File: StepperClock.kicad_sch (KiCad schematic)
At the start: 24 parts, among them J1 Hour1, J2 Hour0, J3 Minute1, J4 Minute0, J5 Second1, J6 Second0, J7 +12V, SW1 TZ, U1 TFT Display, U10 RaspberryPi_Pico, U2 5V, U4 Hour1, U5 Hour0, U6 Min1, U7 Min0, U8 Sec1, U9 Sec0

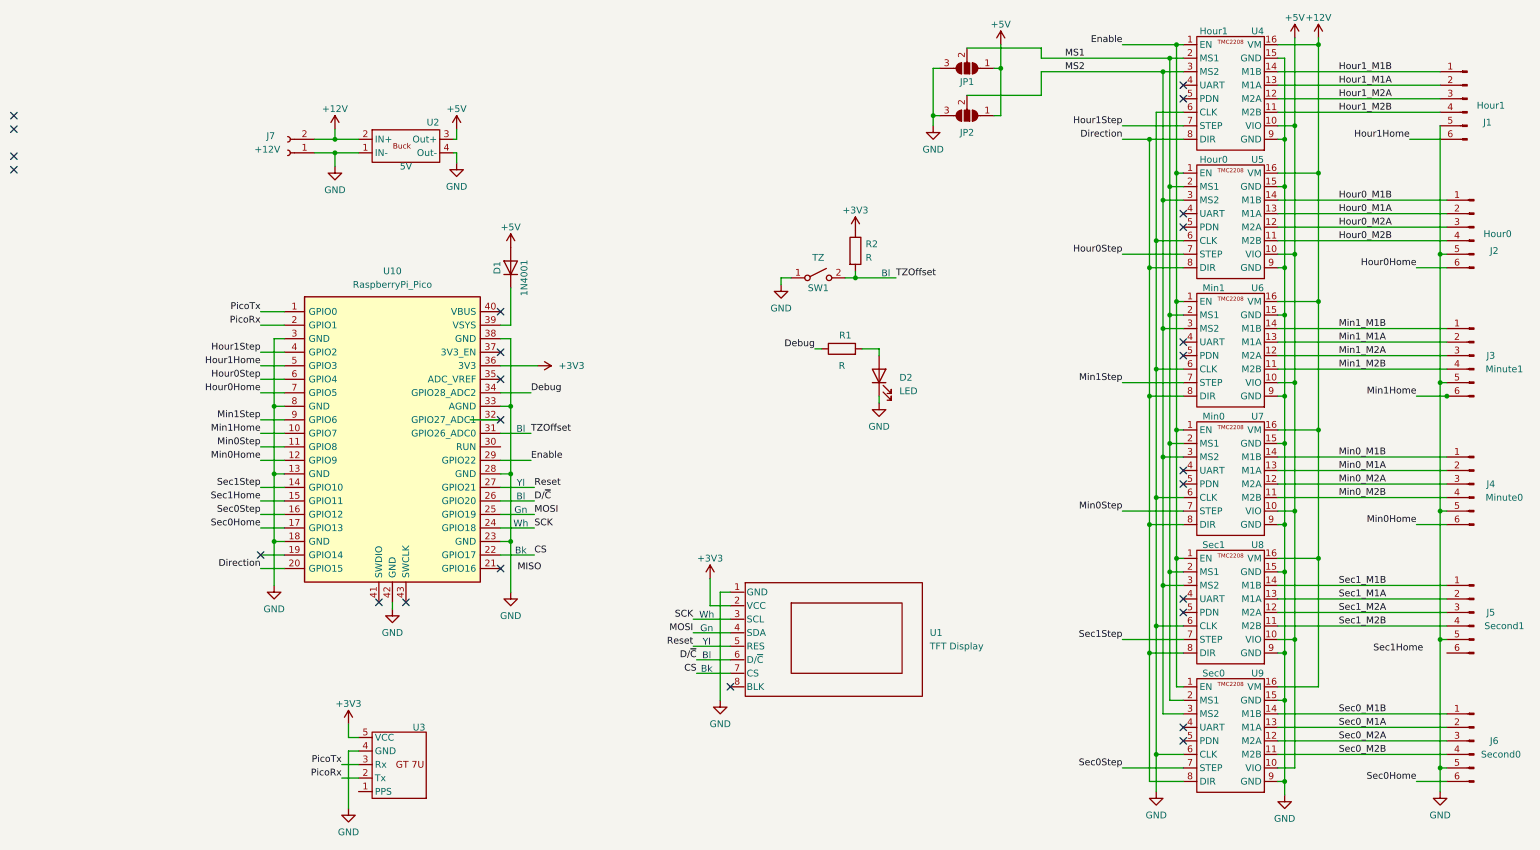
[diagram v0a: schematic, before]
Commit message: Added debug LED and pushbutton
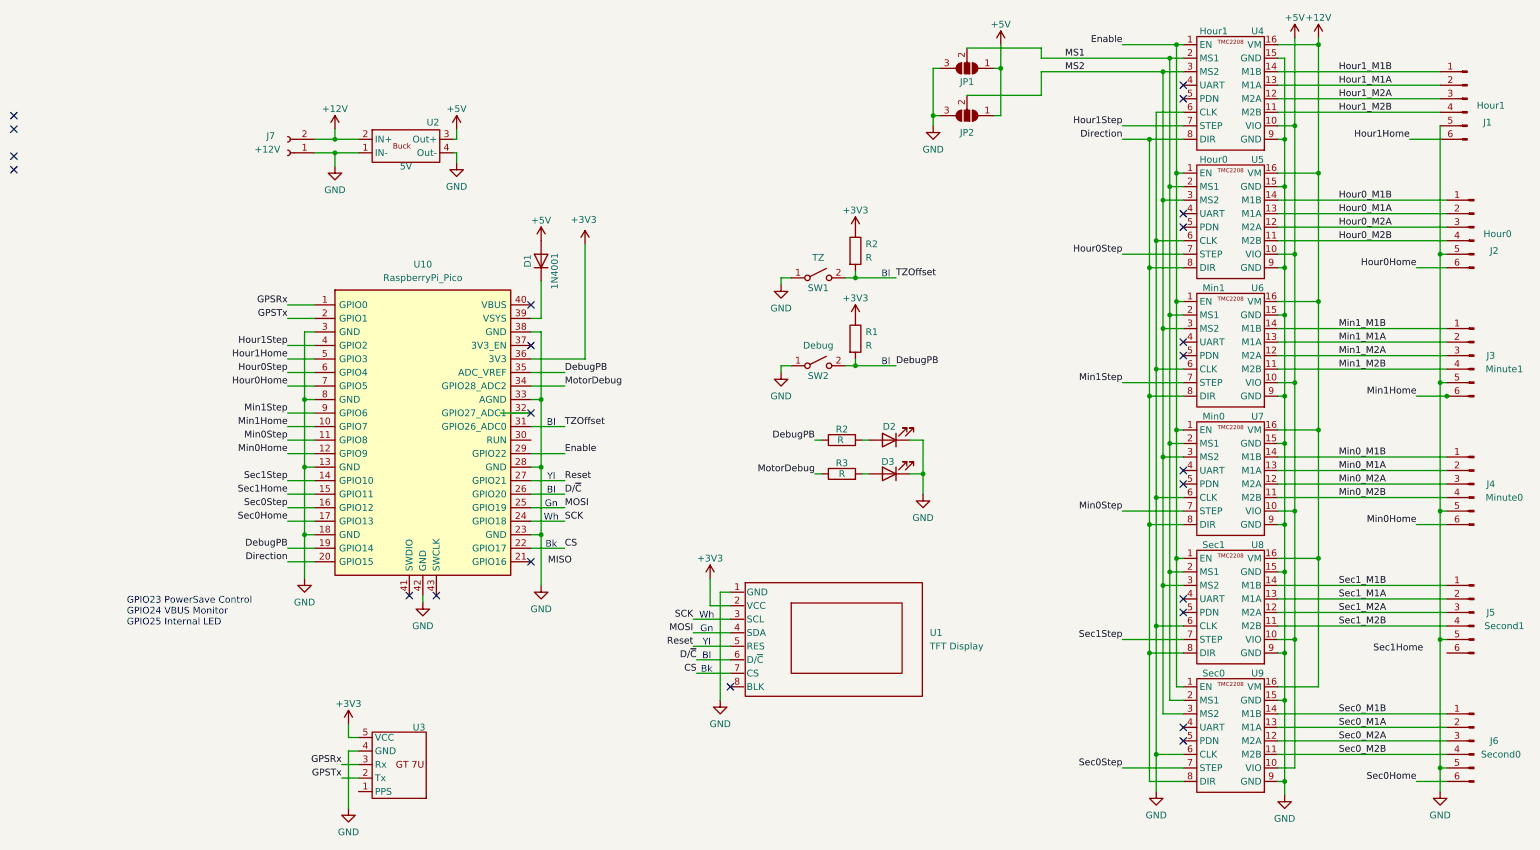
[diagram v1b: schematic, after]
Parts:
- added D3: LED, LED_SMD:LED_miniPLCC_2315_Handsoldering, symbol .tls-symbols:LED
- added R1, R3: R, Resistor_SMD:R_0805_2012Metric_Pad1.20x1.40mm_HandSolder, symbol .tls-symbols:R
- added SW2: Debug, .tls-footprints:SW_PB_Wurth_5x4mm, symbol .tls-symbols:SW_SPST
- renumbered R1 to R2
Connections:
- net +3V3: now also R1.1
- net GND: now also D3.1 (K), SW2.1 (A)
- net DebugPB: now reaches U10.19 (GPIO14)
- net DebugPB: now also R2.1, U10.35 (ADC_VREF), R1.2, SW2.2 (B)
- net Debug renamed MotorDebug
- net MotorDebug: now also R3.1; no longer R2.1
- net PicoRx renamed GPSTx
- net PicoTx renamed GPSRx
- new net: D3.2 (A), R3.2
- no-connect marks 25 -> 23
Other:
- note added: "GPIO23 PowerSave Control GPIO24 VBUS Monitor GPIO25 Internal LED"
- moved on the sheet: D1, D2, R2, U10

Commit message: Remove backup directory from repository Finish board routing
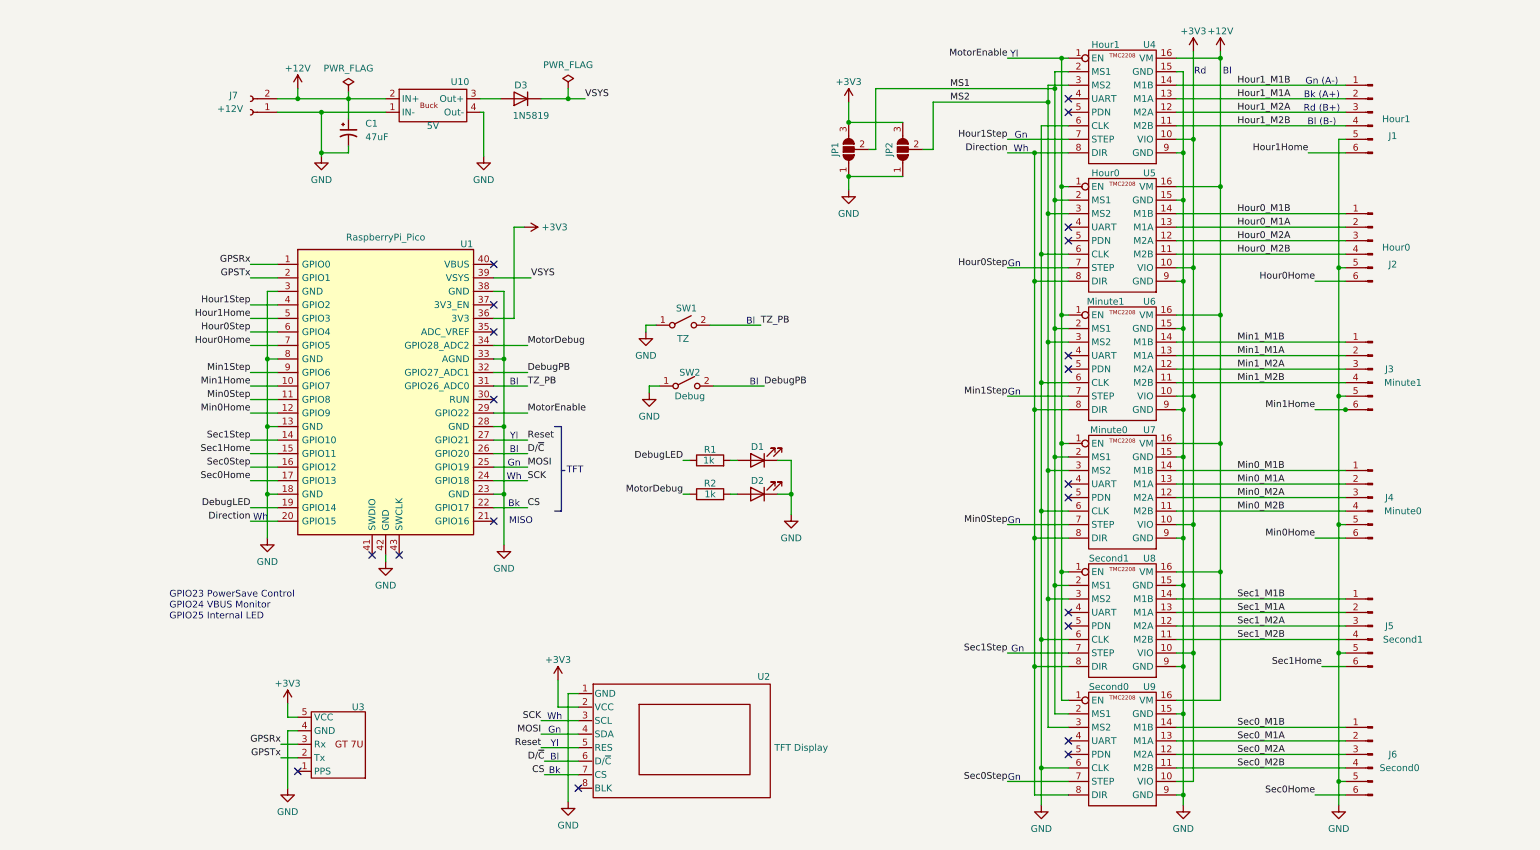
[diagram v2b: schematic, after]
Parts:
- removed D3: LED, LED_SMD:LED_miniPLCC_2315_Handsoldering, symbol .tls-symbols:LED
- removed R1, R2: R, Resistor_SMD:R_0805_2012Metric_Pad1.20x1.40mm_HandSolder, symbol .tls-symbols:R
- removed U10: RaspberryPi_Pico, Module:RaspberryPi_Pico_Common_Unspecified, symbol .tls-symbols:RaspberryPi_Pico
- added C1: 47uF, Capacitor_THT:CP_Radial_D8.0mm_P2.50mm, symbol Device:C_Polarized_Small_US
- added D1: LED, Diode_SMD:D_0805_2012Metric_Pad1.15x1.40mm_HandSolder, symbol .tls-symbols:LED
- added U1: RaspberryPi_Pico, .tls-footprints:RaspberryPi_Pico_Common_THT, symbol .tls-symbols:RaspberryPi_Pico
- D2: footprint LED_SMD:LED_miniPLCC_2315_Handsoldering -> Diode_SMD:D_0805_2012Metric_Pad1.15x1.40mm_HandSolder
- D3: renamed from D1; value 1N4001 -> 1N5819; footprint Diode_THT:D_DO-41_SOD81_P10.16mm_Horizontal -> Diode_THT:D_DO-41_SOD81_P7.62mm_Horizontal
- J7: footprint Connector_PinHeader_1.00mm:PinHeader_1x02_P1.00mm_Vertical -> Connector_PinHeader_2.54mm:PinHeader_1x02_P2.54mm_Vertical
- R1: renamed from R2; value R -> 1k
- R2: renamed from R3; value R -> 1k
- SW1, SW2: footprint .tls-footprints:SW_PB_Wurth_5x4mm -> Button_Switch_THT:SW_PUSH-12mm
- U6: value Min1 -> Minute1
- U7: value Min0 -> Minute0
- U8: value Sec1 -> Second1
- U9: value Sec0 -> Second0
- renumbered U2 to U10, U1 to U2
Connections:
- net +12V: now also C1.1
- net +3V3: now also JP1.3 (B), JP2.3 (B), U4.10 (VIO), U5.10 (VIO), U6.10 (VIO), U7.10 (VIO), U8.10 (VIO), U9.10 (VIO), U1.36 (3V3)
- net CS: now also U1.22 (GPIO17)
- net DebugPB: now also U1.32 (GPIO27_ADC1); no longer R1.1
- net Direction: now also U1.20 (GPIO15)
- net D/~{C}: now also U1.26 (GPIO20)
- net GND: now also JP1.1 (A), JP2.1 (A), C1.2, D1.1 (K), U1.13 (GND), U1.18 (GND), U1.23 (GND), U1.28 (GND), U1.3 (GND), U1.33 (AGND), U1.38 (GND), U1.42 (GND), U1.8 (GND); no longer JP1.3 (B), JP2.3 (B)
- net GPSRx: now also U1.1 (GPIO0)
- net GPSTx: now also U1.2 (GPIO1)
- net Hour0Home: now also U1.7 (GPIO5)
- net Hour0Step: now also U1.6 (GPIO4)
- net Hour1Home: now also U1.5 (GPIO3)
- net Hour1Step: now also U1.4 (GPIO2)
- net MOSI: now also U1.25 (GPIO19)
- net Min0Home: now also U1.12 (GPIO9)
- net Min0Step: now also U1.11 (GPIO8)
- net Min1Home: now also U1.10 (GPIO7)
- net Min1Step: now also U1.9 (GPIO6)
- net MotorDebug: now also U1.34 (GPIO28_ADC2)
- net Reset: now also U1.27 (GPIO21)
- net SCK: now also U1.24 (GPIO18)
- net Sec0Home: now also U1.17 (GPIO13)
- net Sec0Step: now also U1.16 (GPIO12)
- net Sec1Home: now also J5.6 (Pin_6), U1.15 (GPIO11)
- net Sec1Step: now also U1.14 (GPIO10)
- net at R1.2: now also D1.2 (A); no longer D2.2 (A)
- net at R2.2: now also D2.2 (A)
- net VSYS: now reaches D3.1 (K)
- net VSYS: now also U1.39 (VSYS)
- removed net +5V: D3.2 (A), JP1.1 (A), JP2.1 (A), U10.3 (Out+), U4.10 (VIO), U5.10 (VIO), U6.10 (VIO), U7.10 (VIO), U8.10 (VIO), U9.10 (VIO)
- net Enable renamed MotorEnable
- net MotorEnable: now also U1.29 (GPIO22)
- net TZOffset renamed TZ_PB
- net TZ_PB: now also U1.31 (GPIO26_ADC0)
- new net: D3.2 (A), U10.3 (Out+)
- new net DebugLED: R1.1, U1.19 (GPIO14)
- no-connect marks 23 -> 21
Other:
- note added: "Bk (A+)"
- note added: "Bl (B-)"
- note added: "Gn (A-)"
- note added: "MISO"
- note added: "Rd"
- note added: "Rd (B+)"
- note added: "TFT"
- company: (none) -> Salt Creek Software
- title: (none) -> Stepper Clock
- moved on the sheet: D3, J1, J2, J3, J4, J5, J6, J7, JP1, JP2, R1, R2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
